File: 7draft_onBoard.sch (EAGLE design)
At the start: 81 parts, among them IC3 74ABT125PW, IC4 MAX4466KS, J2 USB_MINI-B_DIGIKEY, Q1 NPN 40V 1A SOT-23

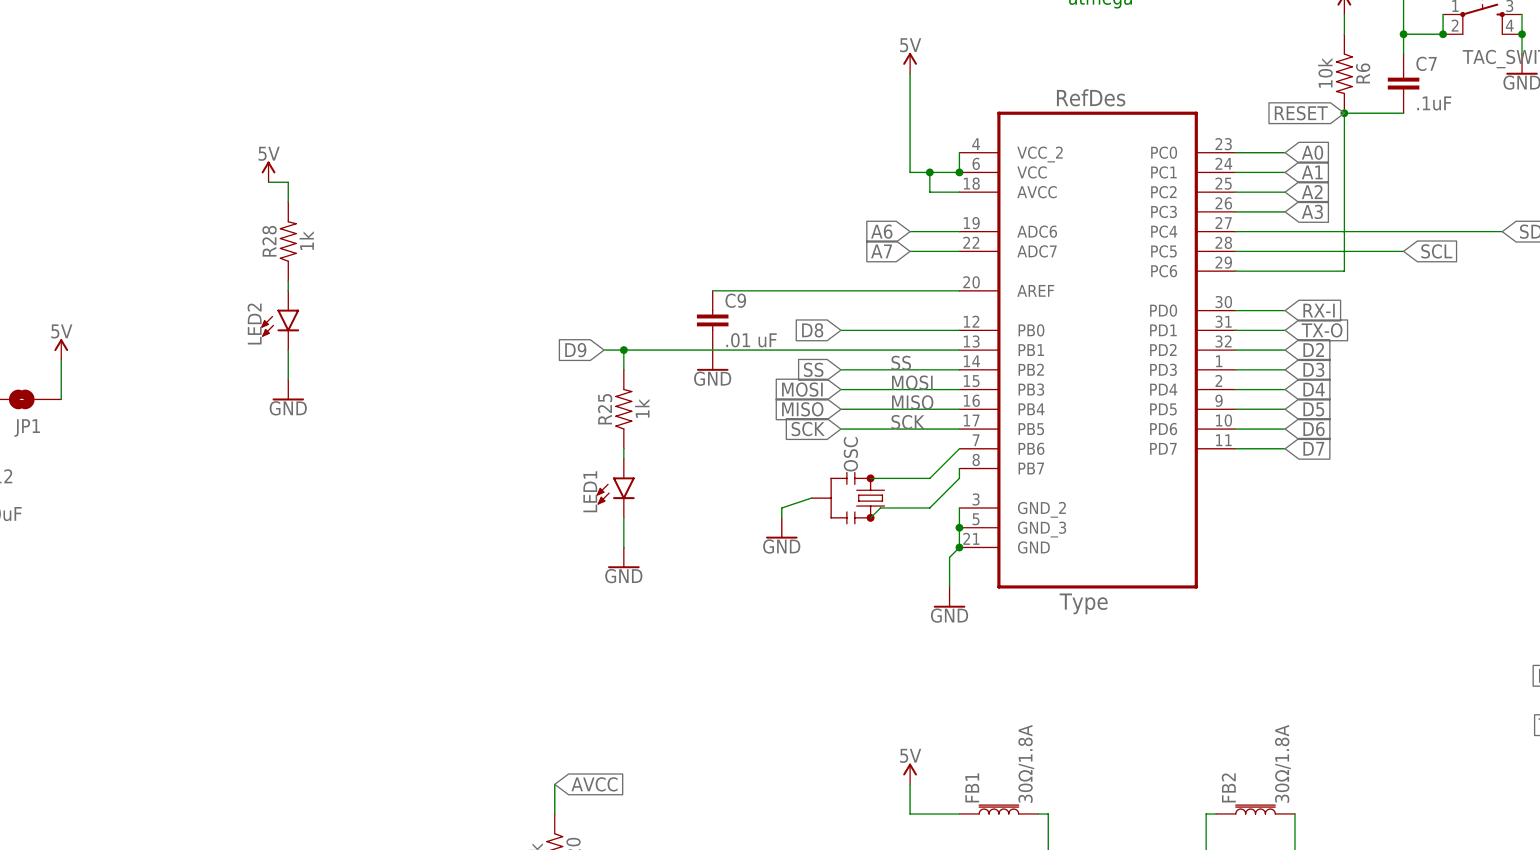
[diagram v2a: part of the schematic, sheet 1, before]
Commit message: less condensed version, indicator leds. and more resistors for IR led
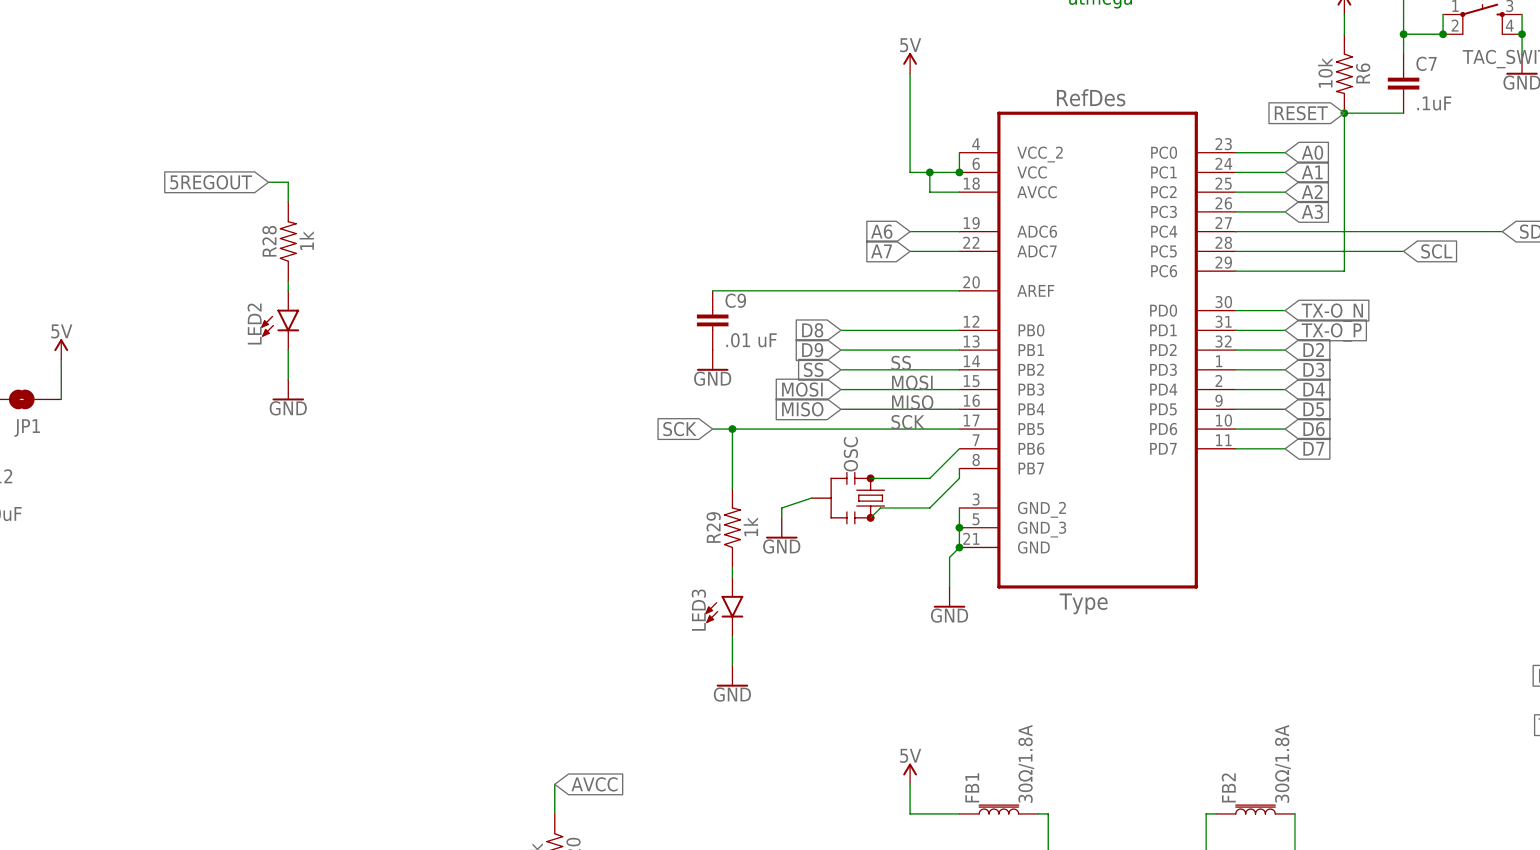
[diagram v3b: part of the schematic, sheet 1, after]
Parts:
- removed LED1: (no value), SparkFun-LED:LED0603
- removed R25: 1k, SparkFun-Retired:2.2MOHM-1/10W-5%(0603)
- added LED3: (no value), SparkFun-LED:LED0603
- added R29: 1k, SparkFun-Retired:2.2MOHM-1/10W-5%(0603)
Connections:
- net N$4 renamed LED4
- net N$5 renamed LED5
- net N$7 renamed POWERLED
- net RX-I renamed TX-O_N
- net TX-O renamed TX-O_P
- removed net N$3: LED1.A, R25.1
- new net N$4: LED3.A, R29.1
- net 5REGOUT: now also R28.2
- net 5V: no longer R28.2
- net D9: no longer R25.2
- net GND: now also LED3.C; no longer LED1.C
- net SCK: now also R29.2
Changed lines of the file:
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@@
 <part name="R23" library="SparkFun-Retired" deviceset="2.2MOHM-1/10W-5%(0603)" device="" value="470"/>
 <part name="R24" library="SparkFun-Retired" deviceset="2.2MOHM-1/10W-5%(0603)" device="" value="470"/>
-<part name="GND3" library="SparkFun-PowerSymbols" deviceset="GND" device=""/>
-<part name="LED1" library="SparkFun-LED" deviceset="LED" device="0603"/>
-<part name="R25" library="SparkFun-Retired" deviceset="2.2MOHM-1/10W-5%(0603)" device="" value="1k"/>
 <part name="LED4" library="SparkFun-LED" deviceset="LED" device="0603"/>
 <part name="R26" library="SparkFun-Retired" deviceset="2.2MOHM-1/10W-5%(0603)" device="" value="1k"/>
@@
 <part name="LED2" library="SparkFun-LED" deviceset="LED" device="0603"/>
 <part name="R28" library="SparkFun-Retired" deviceset="2.2MOHM-1/10W-5%(0603)" device="" value="1k"/>
-<part name="SUPPLY20" library="SparkFun-PowerSymbols" deviceset="5V" device=""/>
+<part name="GND5" library="SparkFun-PowerSymbols" deviceset="GND" device=""/>
+<part name="LED3" library="SparkFun-LED" deviceset="LED" device="0603"/>
+<part name="R29" library="SparkFun-Retired" deviceset="2.2MOHM-1/10W-5%(0603)" device="" value="1k"/>
 </parts>
 <sheets>
@@
 <instance part="R23" gate="G$1" x="-500.38" y="-111.76"/>
 <instance part="R24" gate="G$1" x="-500.38" y="-124.46"/>
-<instance part="GND3" gate="1" x="-364.49" y="66.04"/>
-<instance part="LED1" gate="G$1" x="-364.49" y="77.47"/>
-<instance part="R25" gate="G$1" x="-364.49" y="86.36" rot="R90"/>
 <instance part="LED4" gate="G$1" x="-231.14" y="62.23"/>
 <instance part="R26" gate="G$1" x="-231.14" y="71.12" rot="R90"/>
@@
 <instance part="LED2" gate="G$1" x="-407.67" y="99.06"/>
 <instance part="R28" gate="G$1" x="-407.67" y="107.95" rot="R90"/>
-<instance part="SUPPLY20" gate="G$1" x="-410.21" y="115.57"/>
+<instance part="GND5" gate="1" x="-350.52" y="50.8"/>
+<instance part="LED3" gate="G$1" x="-350.52" y="62.23"/>
+<instance part="R29" gate="G$1" x="-350.52" y="71.12" rot="R90"/>
 </instances>
 <busses>
@@
 <pinref part="SUPPLY19" gate="G$1" pin="5V"/>
 </segment>
-<segment>
-<pinref part="R28" gate="G$1" pin="2"/>
-<wire x1="-407.67" y1="115.57" x2="-410.21" y2="115.57" width="0.1524" layer="91"/>
-<wire x1="-407.67" y1="115.57" x2="-407.67" y2="113.03" width="0.1524" layer="91"/>
-<pinref part="SUPPLY20" gate="G$1" pin="5V"/>
-</segment>
 </net>
 <net name="RESET" class="0">
@@
 </segment>
 </net>
-<net name="RX-I" class="0">
+<net name="TX-O_N" class="0">
 <segment>
 <pinref part="ATMEGA328P-AU" gate="A" pin="PD0"/>
@@
 </segment>
 </net>
-<net name="TX-O" class="0">
+<net name="TX-O_P" class="0">
 <segment>
 <pinref part="ATMEGA328P-AU" gate="A" pin="PD1"/>
@@
 <segment>
 <pinref part="ATMEGA328P-AU" gate="A" pin="PB1"/>
-<label x="-367.03" y="93.98" size="1.778" layer="95" rot="R180" xref="yes"/>
-<wire x1="-321.31" y1="93.98" x2="-364.49" y2="93.98" width="0.1524" layer="91"/>
-<pinref part="R25" gate="G$1" pin="2"/>
-<wire x1="-364.49" y1="93.98" x2="-367.03" y2="93.98" width="0.1524" layer="91"/>
-<wire x1="-364.49" y1="93.98" x2="-364.49" y2="91.44" width="0.1524" layer="91"/>
-<junction x="-364.49" y="93.98"/>
+<label x="-336.55" y="93.98" size="1.778" layer="95" rot="R180" xref="yes"/>
+<wire x1="-321.31" y1="93.98" x2="-336.55" y2="93.98" width="0.1524" layer="91"/>
 </segment>
 <segment>
@@
 <net name="SCK" class="0">
 <segment>
-<pinref part="ATMEGA328P-AU" gate="A" pin="PB5"/>
-<wire x1="-321.31" y1="83.82" x2="-336.55" y2="83.82" width="0.1524" layer="91"/>
-<label x="-336.55" y="83.82" size="1.778" layer="95" rot="R180" xref="yes"/>
-<label x="-330.2" y="83.82" size="1.778" layer="95"/>
-</segment>
-<segment>
 <pinref part="IC3" gate="A" pin="I"/>
 <wire x1="-435.61" y1="222.25" x2="-436.88" y2="222.25" width="0.1524" layer="91"/>
@@
 <wire x1="-170.18" y1="81.28" x2="-175.26" y2="81.28" width="0.1524" layer="91"/>
 <label x="-175.26" y="81.28" size="1.778" layer="95" rot="R180"/>
+</segment>
+<segment>
+<pinref part="R29" gate="G$1" pin="2"/>
+<pinref part="ATMEGA328P-AU" gate="A" pin="PB5"/>
+<wire x1="-321.31" y1="83.82" x2="-350.52" y2="83.82" width="0.1524" layer="91"/>
+<label x="-353.06" y="83.82" size="1.778" layer="95" rot="R180" xref="yes"/>
+<label x="-330.2" y="83.82" size="1.778" layer="95"/>
+<wire x1="-350.52" y1="83.82" x2="-353.06" y2="83.82" width="0.1524" layer="91"/>
+<wire x1="-350.52" y1="76.2" x2="-350.52" y2="83.82" width="0.1524" layer="91"/>
+<junction x="-350.52" y="83.82"/>
 </segment>
 </net>
@@
 </segment>
 <segment>
-<pinref part="LED1" gate="G$1" pin="C"/>
-<pinref part="GND3" gate="1" pin="GND"/>
-<wire x1="-364.49" y1="72.39" x2="-364.49" y2="68.58" width="0.1524" layer="91"/>
-</segment>
-<segment>
 <pinref part="LED2" gate="G$1" pin="C"/>
 <pinref part="GND4" gate="1" pin="GND"/>
 <wire x1="-407.67" y1="93.98" x2="-407.67" y2="90.17" width="0.1524" layer="91"/>
+</segment>
+<segment>
+<pinref part="LED3" gate="G$1" pin="C"/>
+<pinref part="GND5" gate="1" pin="GND"/>
+<wire x1="-350.52" y1="57.15" x2="-350.52" y2="53.34" width="0.1524" layer="91"/>
 </segment>
 </net>
@@
 <wire x1="-447.04" y1="87.63" x2="-448.31" y2="87.63" width="0.1524" layer="91"/>
 <junction x="-448.31" y="87.63"/>
+</segment>
+<segment>
+<pinref part="R28" gate="G$1" pin="2"/>
+<wire x1="-407.67" y1="115.57" x2="-410.21" y2="115.57" width="0.1524" layer="91"/>
+<wire x1="-407.67" y1="115.57" x2="-407.67" y2="113.03" width="0.1524" layer="91"/>
+<label x="-410.21" y="115.57" size="1.778" layer="95" rot="R180" xref="yes"/>
 </segment>
 </net>
@@
 </segment>
 </net>
-<net name="N$3" class="0">
-<segment>
-<pinref part="LED1" gate="G$1" pin="A"/>
-<pinref part="R25" gate="G$1" pin="1"/>
-<wire x1="-364.49" y1="81.28" x2="-364.49" y2="80.01" width="0.1524" layer="91"/>
-</segment>
-</net>
-<net name="N$4" class="0">
+<net name="LED4" class="0">
 <segment>
 <pinref part="R26" gate="G$1" pin="1"/>
@@
 </segment>
 </net>
-<net name="N$5" class="0">
+<net name="LED5" class="0">
 <segment>
 <pinref part="R27" gate="G$1" pin="1"/>
@@
 </segment>
 </net>
-<net name="N$7" class="0">
+<net name="POWERLED" class="0">
 <segment>
 <pinref part="LED2" gate="G$1" pin="A"/>
 <pinref part="R28" gate="G$1" pin="1"/>
 <wire x1="-407.67" y1="102.87" x2="-407.67" y2="101.6" width="0.1524" layer="91"/>
+</segment>
+</net>
+<net name="N$4" class="0">
+<segment>
+<pinref part="LED3" gate="G$1" pin="A"/>
+<pinref part="R29" gate="G$1" pin="1"/>
+<wire x1="-350.52" y1="66.04" x2="-350.52" y2="64.77" width="0.1524" layer="91"/>
 </segment>
 </net>
@@
 </segment>
 </net>
-<net name="RX-I" class="0">
+<net name="TX-O_N" class="0">
 <segment>
 <pinref part="R8" gate="G$1" pin="2"/>
@@
 </segment>
 </net>
-<net name="TX-O" class="0">
+<net name="TX-O_P" class="0">
 <segment>
 <pinref part="R9" gate="G$1" pin="2"/>

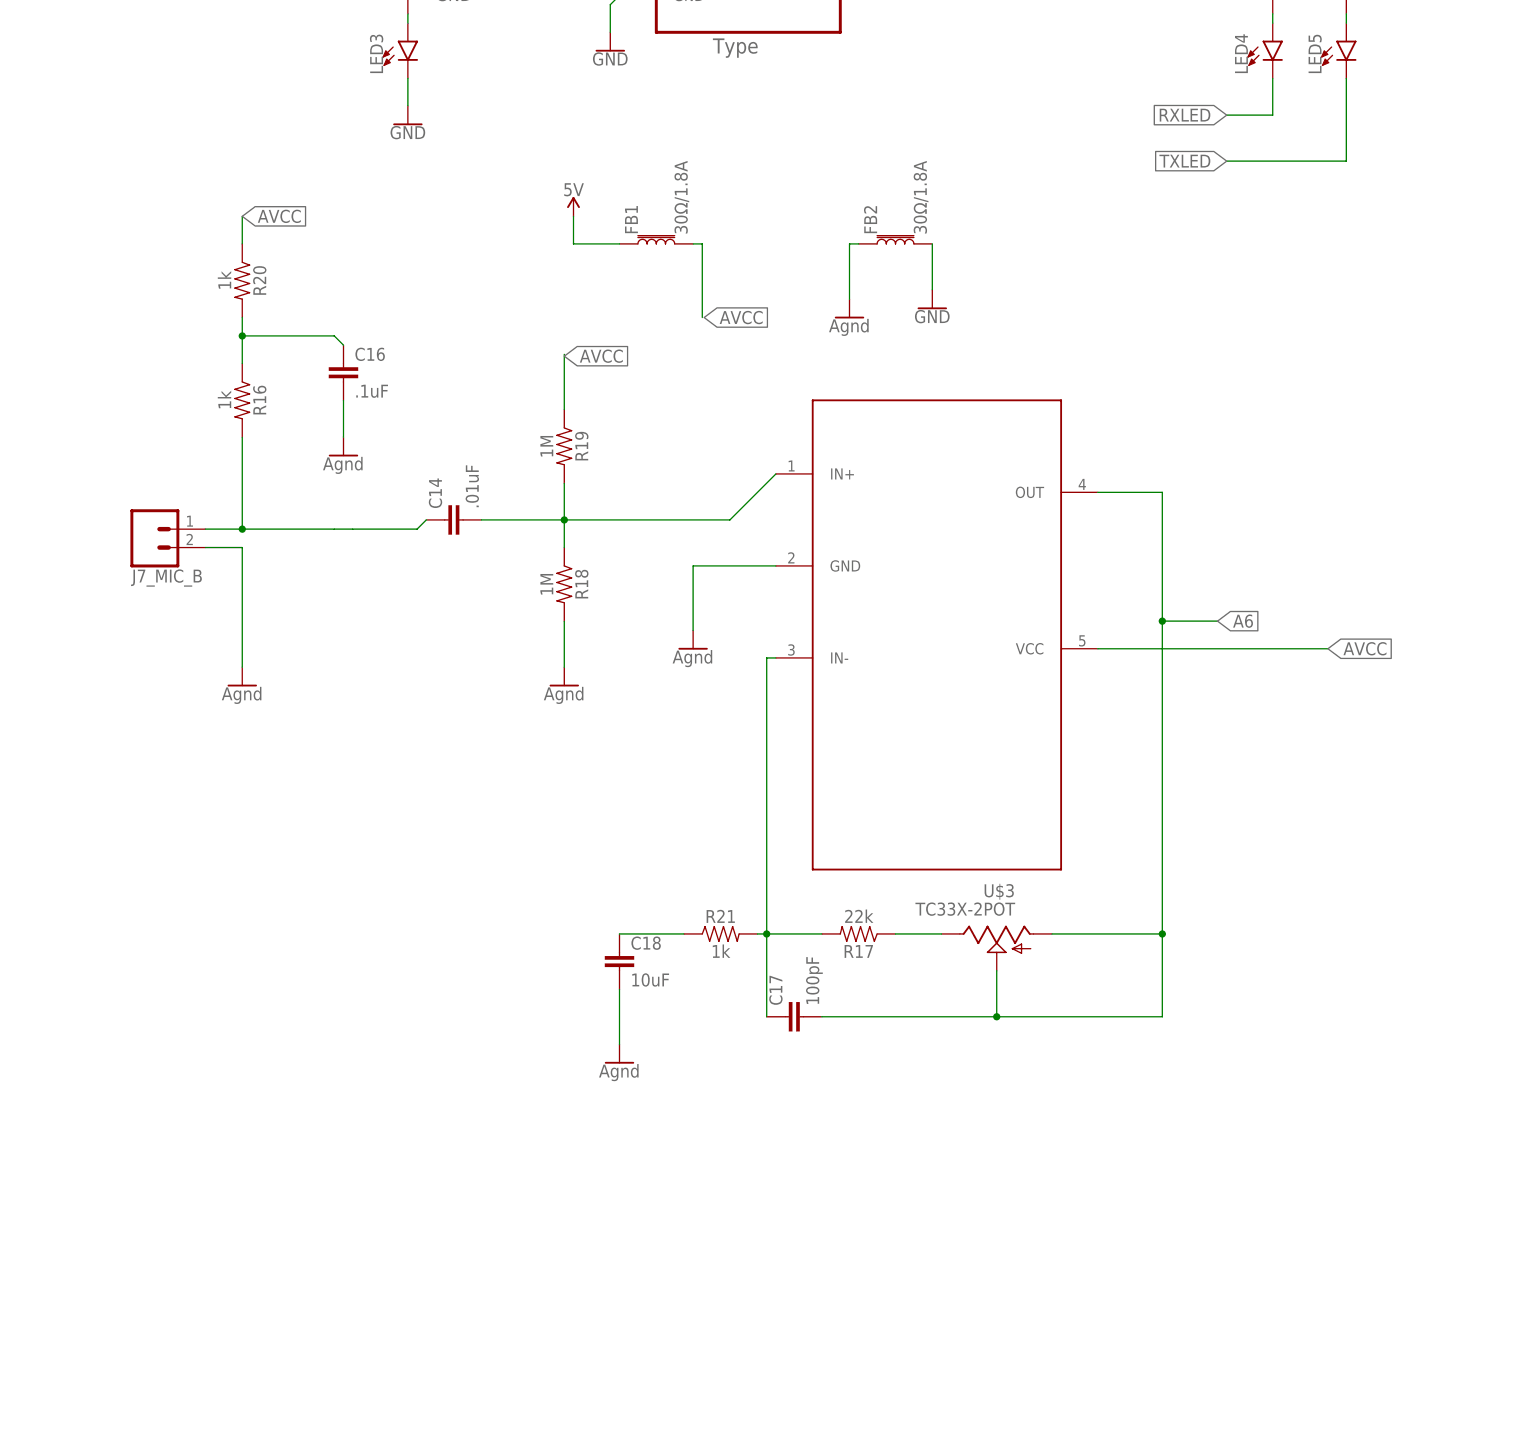
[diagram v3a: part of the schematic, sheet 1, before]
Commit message: Almost done, wanted to save before I change the IR leds to an equivalent resistance or a resistor array.
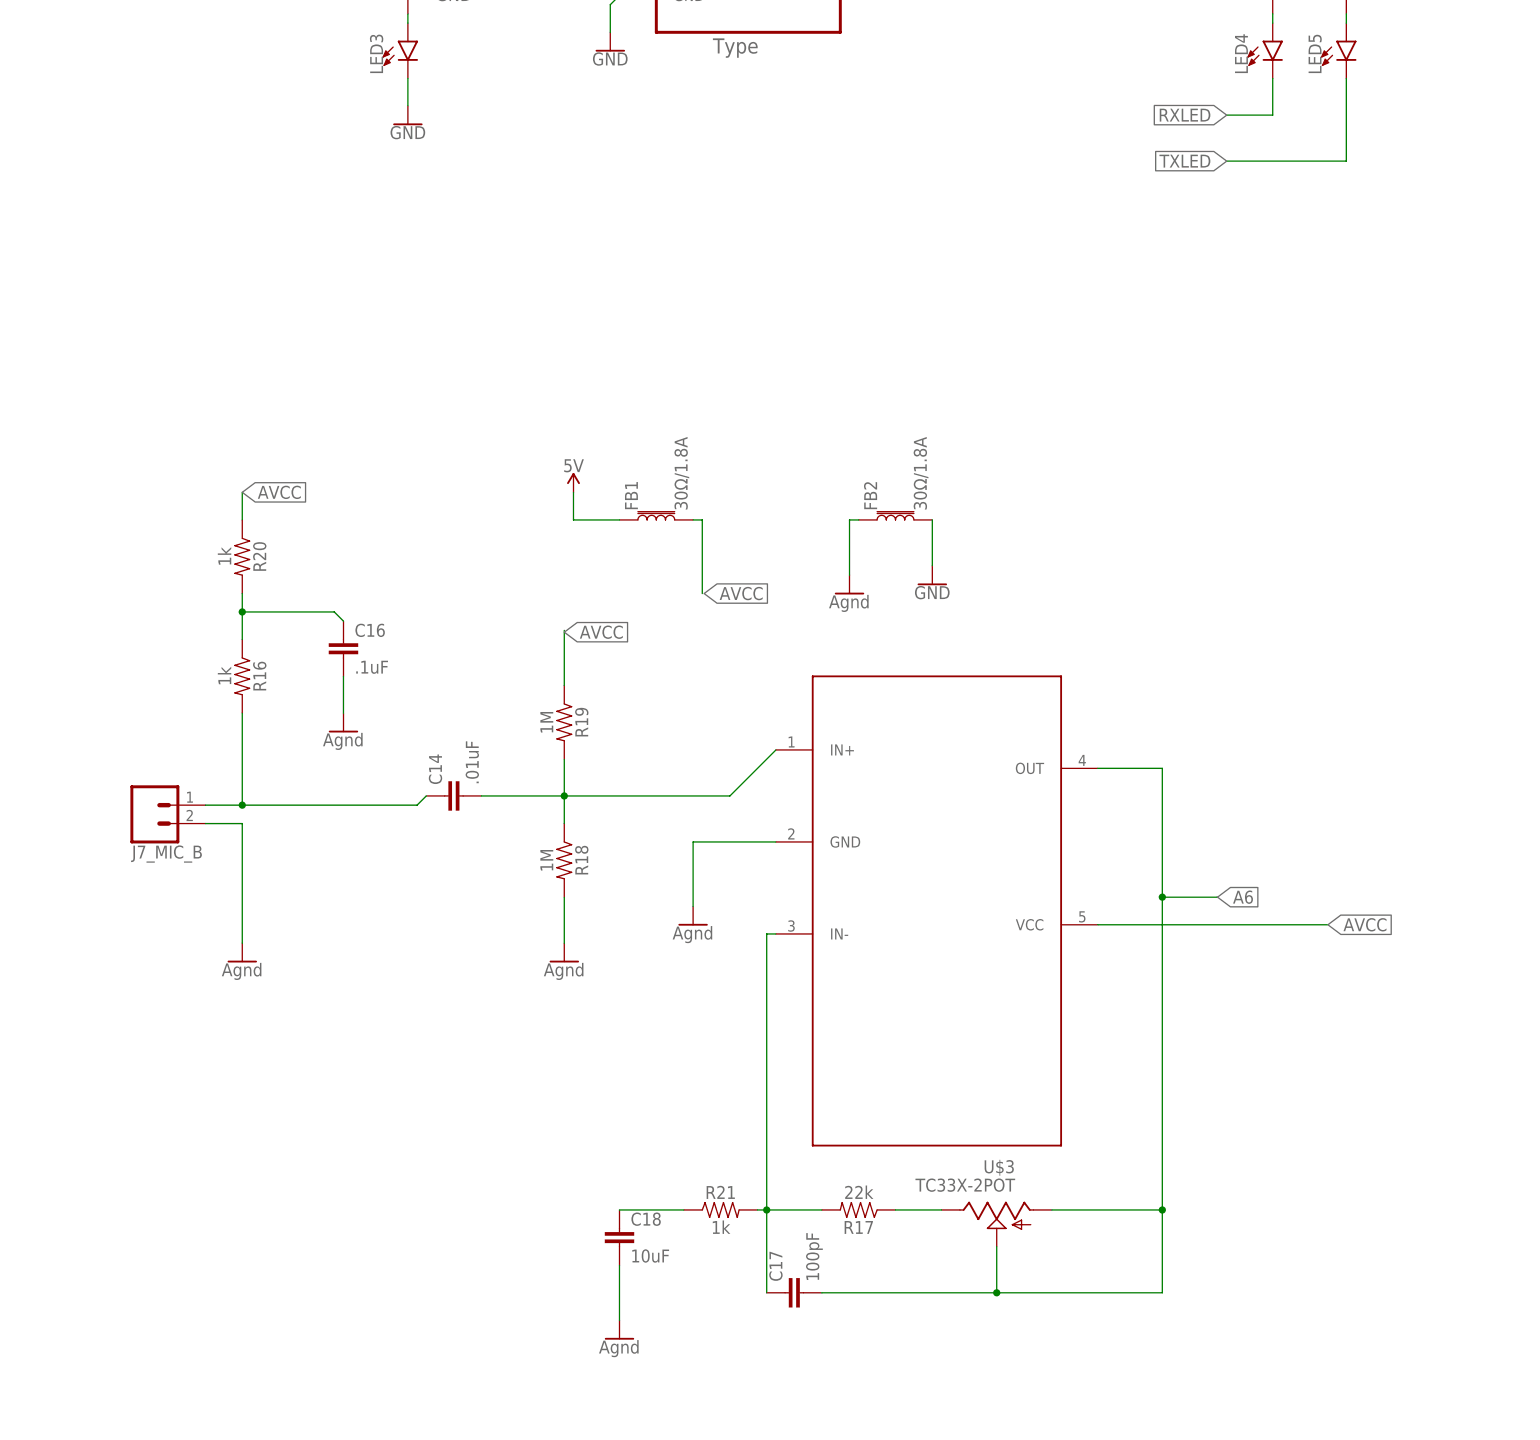
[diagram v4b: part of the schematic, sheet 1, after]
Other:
- moved on the sheet: C14, C16, C17, C18, FB1, FB2, J7_MIC_B, R16, R17, R18, R19, R20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
